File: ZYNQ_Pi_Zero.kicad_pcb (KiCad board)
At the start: 4 copper layers, 59 parts, among them Q501 2N7002, Q502 2N7002, Q503 2N7002, U101 xc7z010clg400, U201 MT41K256M16TW-107_P, U301 W25Q256FVEI, U501 TPD4E05U06DQA, U502 TPD4E05U06DQA

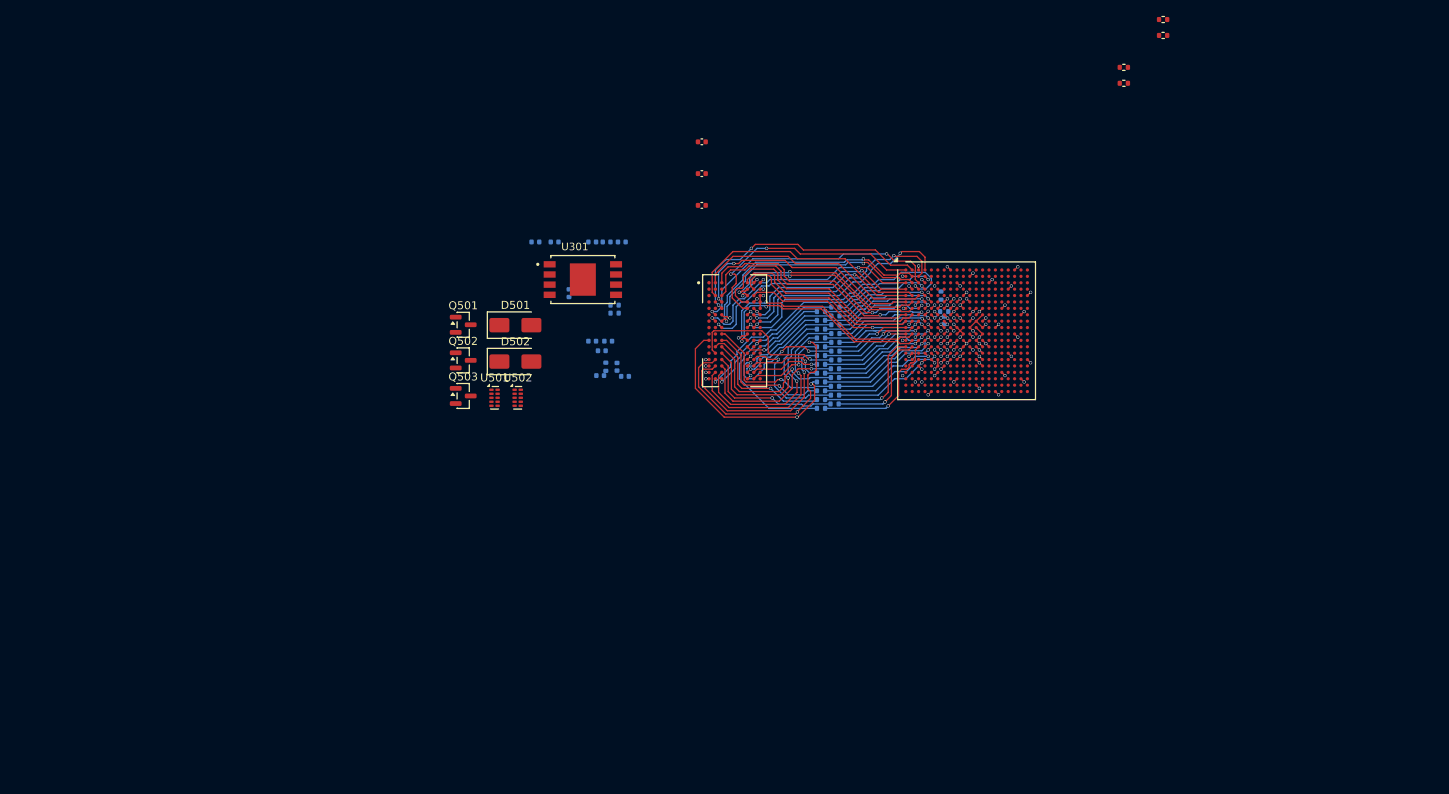
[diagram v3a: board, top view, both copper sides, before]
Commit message: feat: continue routing ddr3
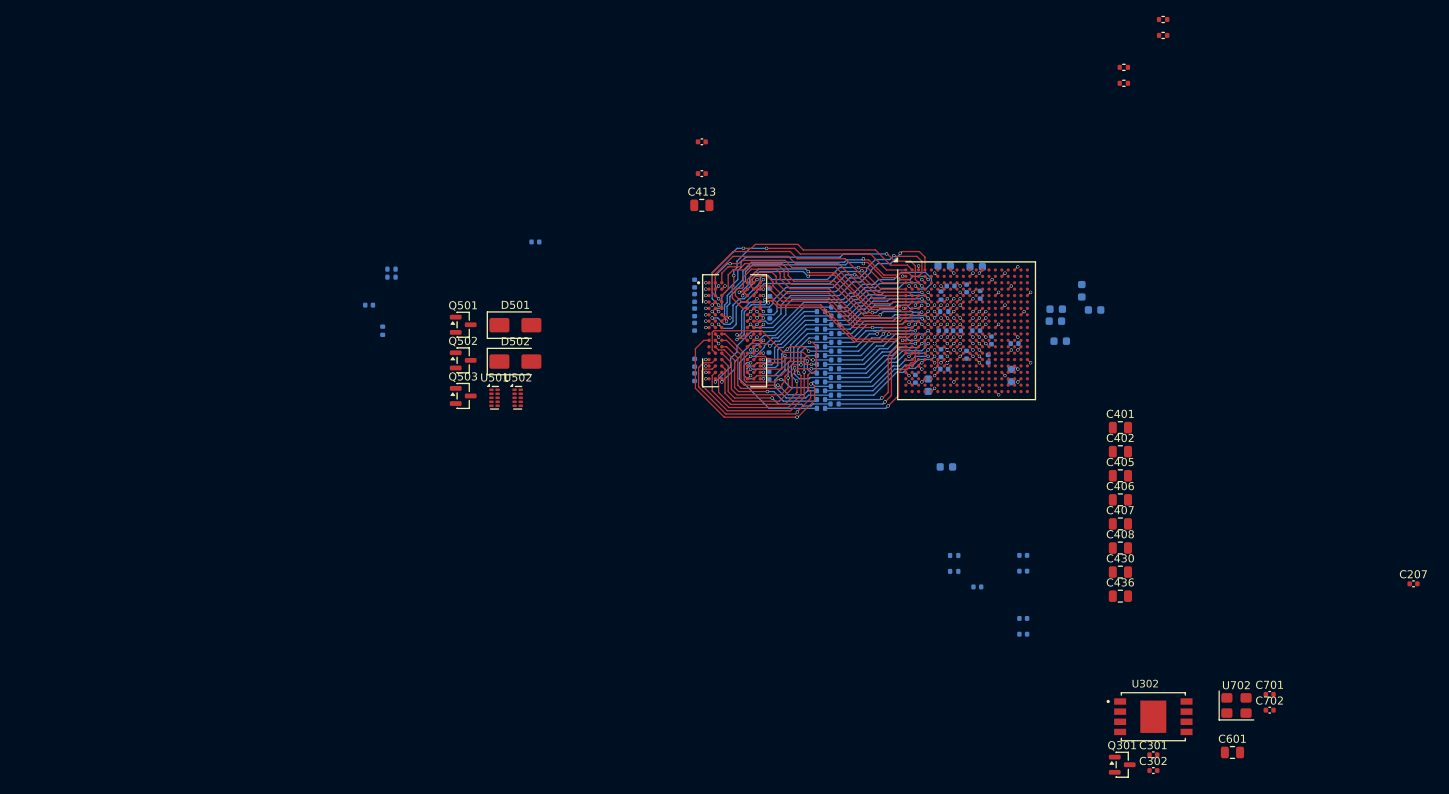
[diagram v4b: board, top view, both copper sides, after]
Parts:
- removed R231: 10R, Resistor_SMD:R_0402_1005Metric
- removed U301: W25Q256FVEI, Footprints:IC_W25N04KVZEIU
- added C207: 100n, Capacitor_SMD:C_0402_1005Metric, F.Cu at (204.9, 131.6)
- added C301: 470n, Capacitor_SMD:C_0402_1005Metric, F.Cu at (172.3, 153.0)
- added C302: 470n, Capacitor_SMD:C_0402_1005Metric, F.Cu at (172.3, 155.0)
- added C401: 10u, Capacitor_SMD:C_0805_2012Metric, F.Cu at (168.2, 112.1)
- added C402: 10u, Capacitor_SMD:C_0805_2012Metric, F.Cu at (168.2, 115.1)
- added C403: 3n3, Capacitor_SMD:C_0402_1005Metric, B.Cu at (156.1, 128.1)
- added C404: 3n3, Capacitor_SMD:C_0402_1005Metric, B.Cu at (156.1, 130.1)
- added C405: 47u, Capacitor_SMD:C_0805_2012Metric, F.Cu at (168.2, 118.1)
- added C406: 10u, Capacitor_SMD:C_0805_2012Metric, F.Cu at (168.2, 121.1)
- added C407: 22u, Capacitor_SMD:C_0805_2012Metric, F.Cu at (168.2, 124.1)
- added C408: 10u, Capacitor_SMD:C_0805_2012Metric, F.Cu at (168.2, 127.2)
- added C409: 4u7, Capacitor_SMD:C_0603_1608Metric, B.Cu at (160.2, 97.3)
- added C410: 4u7, Capacitor_SMD:C_0603_1608Metric, B.Cu at (154.6, 105.6)
- added C411: 470n, Capacitor_SMD:C_0402_1005Metric, B.Cu at (146.2, 104.8)
- added C412: 470n, Capacitor_SMD:C_0402_1005Metric, B.Cu at (155.0, 101.6)
- added C414: 3n3, Capacitor_SMD:C_0402_1005Metric, B.Cu at (156.1, 136.0)
- added C415: 100n, Capacitor_SMD:C_0402_1005Metric, B.Cu at (156.1, 137.9)
- added C416: 4u7, Capacitor_SMD:C_0603_1608Metric, B.Cu at (165.0, 97.4)
- added C417: 4u7, Capacitor_SMD:C_0603_1608Metric, B.Cu at (146.5, 117.0)
- added C418: 470n, Capacitor_SMD:C_0402_1005Metric, B.Cu at (150.2, 100.0)
- added C419: 470n, Capacitor_SMD:C_0402_1005Metric, B.Cu at (149.0, 103.0)
- added C420: 4u7, Capacitor_SMD:C_0603_1608Metric, B.Cu at (160.7, 101.3)
- added C421: 4u7, Capacitor_SMD:C_0603_1608Metric, B.Cu at (146.2, 91.9)
- added C422: 470n, Capacitor_SMD:C_0402_1005Metric, B.Cu at (146.0, 100.0)
- added C423: 470n, Capacitor_SMD:C_0402_1005Metric, B.Cu at (147.0, 94.4)
- added C424: 470n, Capacitor_SMD:C_0402_1005Metric, B.Cu at (145.8, 102.8)
- added C425: 4u7, Capacitor_SMD:C_0603_1608Metric, B.Cu at (160.1, 98.8)
- added C426: 4u7, Capacitor_SMD:C_0603_1608Metric, B.Cu at (150.2, 92.0)
- added C427: 470n, Capacitor_SMD:C_0402_1005Metric, B.Cu at (151.7, 103.5)
- added C428: 470n, Capacitor_SMD:C_0402_1005Metric, B.Cu at (149.0, 94.7)
- added C429: 470n, Capacitor_SMD:C_0402_1005Metric, B.Cu at (152.1, 101.2)
- added C430: 10u, Capacitor_SMD:C_0805_2012Metric, F.Cu at (168.2, 130.2)
- added C431: 470n, Capacitor_SMD:C_0402_1005Metric, B.Cu at (150.3, 132.0)
- added C432: 4u7, Capacitor_SMD:C_0603_1608Metric, B.Cu at (163.4, 95.0)
- added C433: 4u7, Capacitor_SMD:C_0603_1608Metric, B.Cu at (144.2, 106.8)
- added C434: 470n, Capacitor_SMD:C_0402_1005Metric, B.Cu at (147.8, 100.0)
- added C435: 470n, Capacitor_SMD:C_0402_1005Metric, B.Cu at (142.6, 106.0)
- added C436: 22u, Capacitor_SMD:C_0805_2012Metric, F.Cu at (168.2, 133.2)
- added C601: 10u, Capacitor_SMD:C_0805_2012Metric, F.Cu at (182.2, 152.7)
- added C701: 100n, Capacitor_SMD:C_0402_1005Metric, F.Cu at (186.9, 145.5)
- added C702: 470n, Capacitor_SMD:C_0402_1005Metric, F.Cu at (186.9, 147.4)
- added Q301: MMBT3904, Package_TO_SOT_SMD:SOT-23, F.Cu at (168.5, 154.2)
- added R228: 10R, Resistor_SMD:R_0402_1005Metric, B.Cu at (130.8, 106.4)
- added R404: 10k, Resistor_SMD:R_0402_1005Metric, B.Cu at (147.4, 128.1)
- added R409: 10k, Resistor_SMD:R_0402_1005Metric, B.Cu at (147.4, 130.1)
- added U302: W25Q256FVEI, Footprints:IC_W25N04KVZEIU, F.Cu at (172.3, 148.2)
- added U702: 33.3333MHz, Oscillator:Oscillator_SMD_SeikoEpson_SG8002CE-4Pin_3.2x2.5mm, F.Cu at (182.7, 146.8)
- C213: value 100n -> 10n
- C413: value 100n -> 10u; footprint Capacitor_SMD:C_0402_1005Metric -> Capacitor_SMD:C_0805_2012Metric
- R402: value 10k -> 5k1
- R407: value 10k -> 13k
- moved C203 31.6 mm to (124.3, 105.6), turned to -90 degrees
- moved C214 28.3 mm to (74.3, 96.8)
- moved R201 28.3 mm to (76.0, 100.0)
- moved R202 28.3 mm to (77.1, 93.3)
- moved R203 28.3 mm to (77.1, 92.3)
- moved C205 23.1 mm to (124.4, 95.2), turned to 90 degrees
- moved C210 21.5 mm to (124.4, 98.0), turned to -90 degrees
- moved C209 20.2 mm to (124.3, 103.2), turned to 90 degrees
- moved C212 18.9 mm to (115.0, 105.8)
- moved C204 14.2 mm to (115.0, 97.7), turned to -90 degrees
- moved C202 12.2 mm to (115.0, 94.1), turned to 90 degrees
- moved C201 11.5 mm to (115.0, 95.9), turned to -90 degrees
- moved C206 10.9 mm to (115.0, 99.5)
- moved C211 8.86 mm to (115.0, 104.0), turned to -90 degrees
- moved C208 5.52 mm to (150.7, 95.5)
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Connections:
- net /POWER/1V5_PG renamed Net-(J401-CC2)
- C205 pad 2: VTTREF -> GND
- C206 pad 1: VTTREF -> +1V5
- C213 pad 1: +1V5 -> VTTREF
- C214 pad 1: +1V5 -> VTTREF
- R229 pad 1: /DDR3/PS_DDR_ODT -> /DDR3/PS_DDR_~{WE}
- R229 pad 2: /DDR3/DDR_ODT -> /DDR3/DDR_~{WE}
- R230 pad 1: /DDR3/PS_DDR_~{WE} -> /DDR3/PS_DDR_~{RAS}
- R230 pad 2: /DDR3/DDR_~{WE} -> /DDR3/DDR_~{RAS}
- R402 pad 2: +5V -> GND
- R407 pad 1: /POWER/1V8_PG -> +1V5
- R407 pad 2: +5V -> Net-(U402-FB)
- U101 pad A10: (no net) -> unconnected-(U101F-PS_MIO37_501-PadA10)
- U101 pad A11: (no net) -> unconnected-(U101F-PS_MIO36_501-PadA11)
- U101 pad A12: (no net) -> unconnected-(U101F-PS_MIO34_501-PadA12)
- U101 pad A13: (no net) -> +1V8
- U101 pad A14: (no net) -> unconnected-(U101F-PS_MIO32_501-PadA14)
- U101 pad A15: (no net) -> unconnected-(U101F-PS_MIO26_501-PadA15)
- U101 pad A16: (no net) -> unconnected-(U101F-PS_MIO24_501-PadA16)
- U101 pad A17: (no net) -> unconnected-(U101F-PS_MIO20_501-PadA17)
- U101 pad A19: (no net) -> unconnected-(U101F-PS_MIO16_501-PadA19)
- U101 pad A5: (no net) -> Net-(U101E-PS_MIO6_500)
- U101 pad A6: (no net) -> QSPI_D3_PS_MIO5
- U101 pad A7: (no net) -> QSPI_CS
- U101 pad A9: (no net) -> SD_DATA1
- U101 pad B10: (no net) -> PS_SRST_B
- U101 pad B12: (no net) -> unconnected-(U101F-PS_MIO48_501-PadB12)
- U101 pad B13: (no net) -> unconnected-(U101F-PS_MIO50_501-PadB13)
- U101 pad B14: (no net) -> unconnected-(U101F-PS_MIO47_501-PadB14)
- U101 pad B15: (no net) -> SD_DATA3
- U101 pad B16: (no net) -> +1V8
- U101 pad B17: (no net) -> unconnected-(U101F-PS_MIO22_501-PadB17)
- U101 pad B18: (no net) -> unconnected-(U101F-PS_MIO18_501-PadB18)
- U101 pad B5: (no net) -> PS_MIO9
- U101 pad B6: (no net) -> +3V3
- U101 pad B7: (no net) -> QSPI_D2_PS_MIO4
- U101 pad B8: (no net) -> QSPI_D0
- U101 pad B9: (no net) -> unconnected-(U101F-PS_MIO51_501-PadB9)
- U101 pad C10: (no net) -> unconnected-(U101F-PS_MIO52_501-PadC10)
- U101 pad C11: (no net) -> unconnected-(U101F-PS_MIO53_501-PadC11)
- U101 pad C12: (no net) -> unconnected-(U101F-PS_MIO49_501-PadC12)
- U101 pad C13: (no net) -> unconnected-(U101F-PS_MIO29_501-PadC13)
- U101 pad C15: (no net) -> unconnected-(U101F-PS_MIO30_501-PadC15)
- U101 pad C16: (no net) -> unconnected-(U101F-PS_MIO28_501-PadC16)
- U101 pad C17: (no net) -> SD_CMD
- U101 pad C18: (no net) -> unconnected-(U101F-PS_MIO39_501-PadC18)
- U101 pad C19: Net-(U101D-VCCO_35[6]-PadC19) -> +1V8
- U101 pad C5: (no net) -> PS_MIO14
- U101 pad C6: (no net) -> PS_MIO11
- U101 pad C7: (no net) -> PS_POR_B
- U101 pad C8: (no net) -> PS_MIO15
- U101 pad D10: (no net) -> unconnected-(U101F-PS_MIO19_501-PadD10)
- U101 pad D11: (no net) -> unconnected-(U101F-PS_MIO23_501-PadD11)
- U101 pad D12: (no net) -> +1V8
- U101 pad D13: (no net) -> unconnected-(U101F-PS_MIO27_501-PadD13)
- U101 pad D14: (no net) -> Net-(U101F-PS_MIO40_501)
- U101 pad D15: (no net) -> unconnected-(U101F-PS_MIO33_501-PadD15)
- U101 pad D16: (no net) -> unconnected-(U101F-PS_MIO46_501-PadD16)
- U101 pad D5: (no net) -> PS_MIO8
- U101 pad D6: (no net) -> QSPI_D1
- U101 pad D7: (no net) -> +3V3
- U101 pad D8: (no net) -> PS_MIO7
- U101 pad D9: (no net) -> PS_MIO12
- U101 pad E11: (no net) -> Net-(U101F-PS_MIO_VREF_501)
- U101 pad E12: (no net) -> SD_DATA0
- U101 pad E13: (no net) -> unconnected-(U101F-PS_MIO38_501-PadE13)
- U101 pad E14: (no net) -> unconnected-(U101F-PS_MIO17_501-PadE14)
- U101 pad E15: (no net) -> +1V8
- U101 pad E16: (no net) -> unconnected-(U101F-PS_MIO31_501-PadE16)
- U101 pad E6: (no net) -> PS_MIO0
- U101 pad E7: (no net) -> PS_CLK
- U101 pad E8: (no net) -> PS_MIO13
- U101 pad E9: (no net) -> PS_MIO10
- U101 pad F12: (no net) -> unconnected-(U101F-PS_MIO35_501-PadF12)
- U101 pad F13: (no net) -> SD_DATA2
- U101 pad F14: (no net) -> unconnected-(U101F-PS_MIO21_501-PadF14)
- U101 pad F15: (no net) -> unconnected-(U101F-PS_MIO25_501-PadF15)
- U101 pad F18: Net-(U101D-VCCO_35[6]-PadC19) -> +1V8
- U101 pad H14: Net-(U101D-VCCO_35[6]-PadC19) -> +1V8
- U101 pad J17: Net-(U101D-VCCO_35[6]-PadC19) -> +1V8
- U101 pad K20: Net-(U101D-VCCO_35[6]-PadC19) -> +1V8
- U101 pad M16: Net-(U101D-VCCO_35[6]-PadC19) -> +1V8
- U101 pad N19: Net-(U101C-VCCO_34[6]-PadN19) -> +3V3
- U101 pad R15: Net-(U101C-VCCO_34[6]-PadN19) -> +3V3
- U101 pad T18: Net-(U101C-VCCO_34[6]-PadN19) -> +3V3
- U101 pad T8: Net-(U101B-VCCO_13[4]-PadT8) -> +3V3
- U101 pad U11: Net-(U101B-VCCO_13[4]-PadT8) -> +3V3
- U101 pad V14: Net-(U101C-VCCO_34[6]-PadN19) -> +3V3
- U101 pad W17: Net-(U101C-VCCO_34[6]-PadN19) -> +3V3
- U101 pad W7: Net-(U101B-VCCO_13[4]-PadT8) -> +3V3
- U101 pad Y10: Net-(U101B-VCCO_13[4]-PadT8) -> +3V3
- U101 pad Y20: Net-(U101C-VCCO_34[6]-PadN19) -> +3V3
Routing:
- net +1V5: track 8.14 -> 14.4 mm, vias 16 -> 28
- net GND: track 45.6 -> 49.2 mm, vias 58 -> 74
- net +3V3: track 3.06 -> 5.33 mm, vias 4 -> 8
- net +1V8: track 6.79 -> 9.05 mm, vias 10 -> 14
- net /DDR3/DDR_BA1: track 14.8 -> 16.6 mm
- net /DDR3/DDR_D12: track 22.9 -> 24.2 mm
- net +1V0: track 9.62 -> 8.49 mm, vias 11 -> 12
- net /DDR3/DDR_BA0: track 20.4 -> 19.3 mm
- net /DDR3/DDR_CLK_N: track 28.4 -> 29.5 mm
- net /DDR3/DDR_D7: track 24.3 -> 23.2 mm
- net /DDR3/DDR_A14: track 13.1 -> 14.1 mm
- net VTTREF: track 1.13 -> 2.10 mm, vias 2 -> 4
- net /DDR3/DDR_CKE: track 17.1 -> 18.0 mm
- net /DDR3/DDR_A11: track 13.2 -> 14.1 mm
- net /DDR3/DDR_D6: track 30.0 -> 30.8 mm
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
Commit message: feat: continue routing
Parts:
- added D301: LED, LED_SMD:LED_0603_1608Metric, F.Cu at (36.5, 87.1)
- added D302: LED, LED_SMD:LED_0603_1608Metric, F.Cu at (36.5, 89.6)
- added D701: LED, LED_SMD:LED_0603_1608Metric, F.Cu at (39.4, 94.2)
- added D801: LED, LED_SMD:LED_0603_1608Metric, F.Cu at (45.4, 94.2)
- added R206: 80R6, Resistor_SMD:R_0402_1005Metric, F.Cu at (136.5, 101.7)
- added R301: 1k, Resistor_SMD:R_0402_1005Metric, F.Cu at (35.9, 78.8)
- added R302: 330R, Resistor_SMD:R_0402_1005Metric, F.Cu at (35.9, 80.8)
- added R303: 1k, Resistor_SMD:R_0402_1005Metric, F.Cu at (35.9, 82.8)
- added R304: 4k7, Resistor_SMD:R_0402_1005Metric, F.Cu at (35.9, 84.8)
- added R305: 4k7, Resistor_SMD:R_0402_1005Metric, F.Cu at (38.8, 78.8)
- added R306: 390R, Resistor_SMD:R_0402_1005Metric, F.Cu at (38.8, 80.8)
- added R307: 470R, Resistor_SMD:R_0402_1005Metric, F.Cu at (38.8, 82.8)
- added R308: 20k, Resistor_SMD:R_0402_1005Metric, F.Cu at (38.8, 84.8)
- added R309: 20k, Resistor_SMD:R_0402_1005Metric, F.Cu at (41.7, 78.8)
- added R310: 20k, Resistor_SMD:R_0402_1005Metric, F.Cu at (41.7, 80.8)
- added R311: 20k, Resistor_SMD:R_0402_1005Metric, F.Cu at (41.7, 82.8)
- added R312: 20k, Resistor_SMD:R_0402_1005Metric, F.Cu at (41.7, 84.8)
- added R313: 20k, Resistor_SMD:R_0402_1005Metric, F.Cu at (44.6, 78.8)
- added R314: 20k, Resistor_SMD:R_0402_1005Metric, F.Cu at (44.6, 80.8)
- added R315: 20k, Resistor_SMD:R_0402_1005Metric, F.Cu at (44.6, 82.8)
- added R316: 20k, Resistor_SMD:R_0402_1005Metric, F.Cu at (44.6, 84.8)
- added R401: 100k, Resistor_SMD:R_0402_1005Metric, F.Cu at (31.0, 78.8)
- added R403: 5k1, Resistor_SMD:R_0402_1005Metric, F.Cu at (31.0, 80.8)
- added R405: 86k6, Resistor_SMD:R_0402_1005Metric, F.Cu at (31.0, 82.8)
- added R406: 200k, Resistor_SMD:R_0402_1005Metric, F.Cu at (31.0, 84.8)
- added R408: 15k, Resistor_SMD:R_0402_1005Metric, F.Cu at (31.0, 86.8)
- added R410: 18k7, Resistor_SMD:R_0402_1005Metric, F.Cu at (31.0, 88.7)
- added R411: 15k, Resistor_SMD:R_0402_1005Metric, F.Cu at (31.0, 90.7)
- added R506: 4k7, Resistor_SMD:R_0402_1005Metric, F.Cu at (49.5, 78.8)
- added R508: 4k7, Resistor_SMD:R_0402_1005Metric, F.Cu at (49.5, 80.8)
- added R513: 4k7, Resistor_SMD:R_0402_1005Metric, F.Cu at (49.5, 82.8)
- added R514: 4k7, Resistor_SMD:R_0402_1005Metric, F.Cu at (49.5, 84.8)
- added R518: 4k7, Resistor_SMD:R_0402_1005Metric, F.Cu at (49.5, 86.8)
- added R701: 1k, Resistor_SMD:R_0402_1005Metric, F.Cu at (35.9, 93.9)
- added R708: 1k, Resistor_SMD:R_0402_1005Metric, F.Cu at (35.9, 95.9)
- added R709: 1k, Resistor_SMD:R_0402_1005Metric, F.Cu at (35.9, 97.9)
- added R801: 1k, Resistor_SMD:R_0402_1005Metric, F.Cu at (44.8, 96.5)
- C207: moved to B.Cu
- moved C207 91.2 mm to (118.7, 101.7), turned to -90 degrees
- moved R203 40.3 mm to (116.4, 101.3)
- moved R202 39.9 mm to (116.4, 100.4)
- moved R201 37.9 mm to (113.9, 100.9)
- moved C208 33.9 mm to (117.6, 102.7)
- moved R207 1.60 mm to (134.1, 109.2)
- moved R208 1.60 mm to (134.2, 102.5)
- moved R209 1.60 mm to (134.2, 104.8)
- moved R210 1.60 mm to (134.2, 101.5)
- moved R211 1.60 mm to (132.4, 105.3)
- moved R212 1.60 mm to (132.4, 103.1)
- moved R213 1.60 mm to (132.4, 104.2)
- moved R214 1.60 mm to (132.4, 100.9)
- moved R215 1.60 mm to (132.4, 102.0)
- moved R216 1.60 mm to (134.2, 100.3)
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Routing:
- net VTTREF: track 2.10 -> 10.3 mm
- net /DDR3/DDR_A11: track 14.1 -> 20.1 mm
- net /DDR3/DDR_A1: track 16.8 -> 21.2 mm
- net /DDR3/DDR_A3: track 32.3 -> 36.5 mm
- net /DDR3/DDR_A9: track 25.1 -> 28.8 mm
- net /DDR3/DDR_BA2: track 22.3 -> 25.4 mm
- net /DDR3/DDR_A7: track 23.9 -> 27.0 mm
- net /DDR3/DDR_A14: track 14.1 -> 16.8 mm
- net /DDR3/DDR_A5: track 25.1 -> 27.6 mm
- net /DDR3/DDR_ODT: track 27.5 -> 29.5 mm
- net /DDR3/DDR_CKE: track 18.0 -> 19.9 mm
- net /DDR3/PS_DDR_A3: track 10.9 -> 9.06 mm
- net /DDR3/DDR_~{RAS}: track 18.7 -> 20.4 mm
- net /DDR3/DDR_A2: track 19.9 -> 21.6 mm
- net /DDR3/PS_DDR_A13: track 12.3 -> 10.7 mm
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
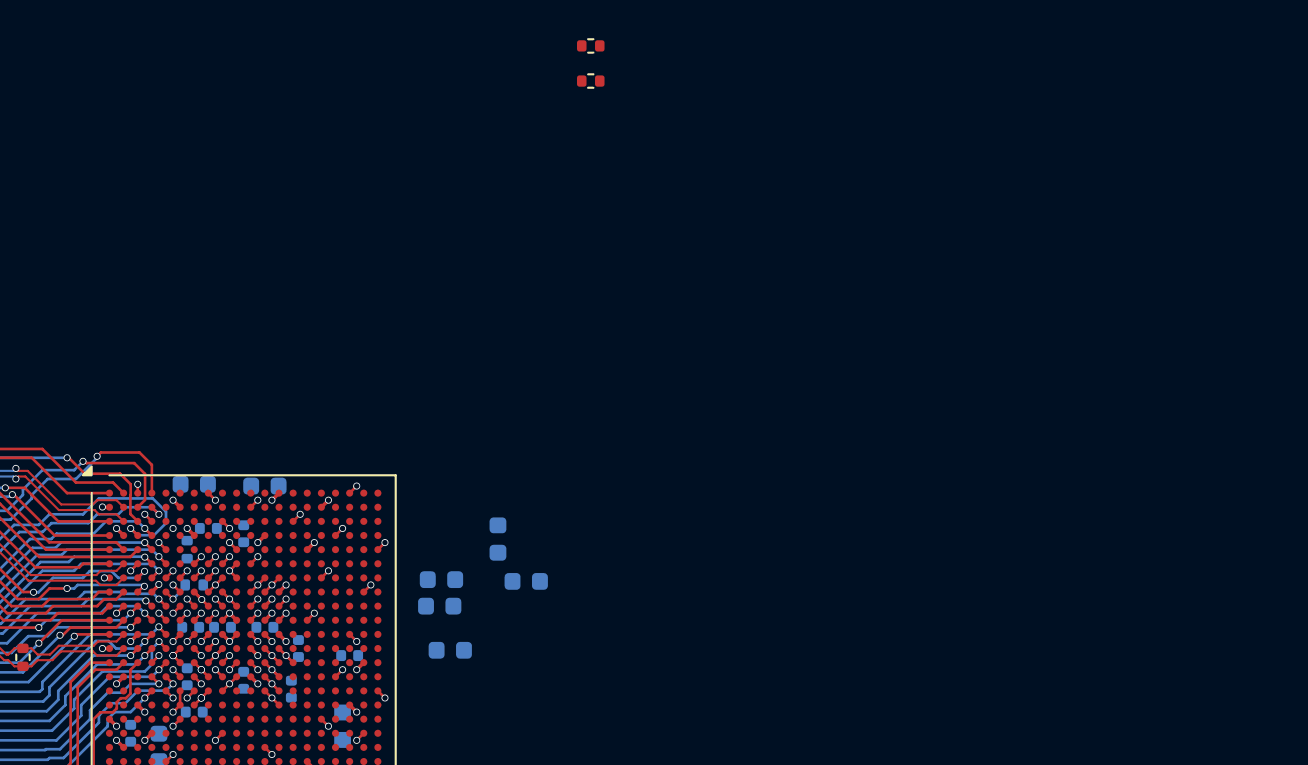
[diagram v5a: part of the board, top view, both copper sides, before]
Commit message: feat: add sd card footprint
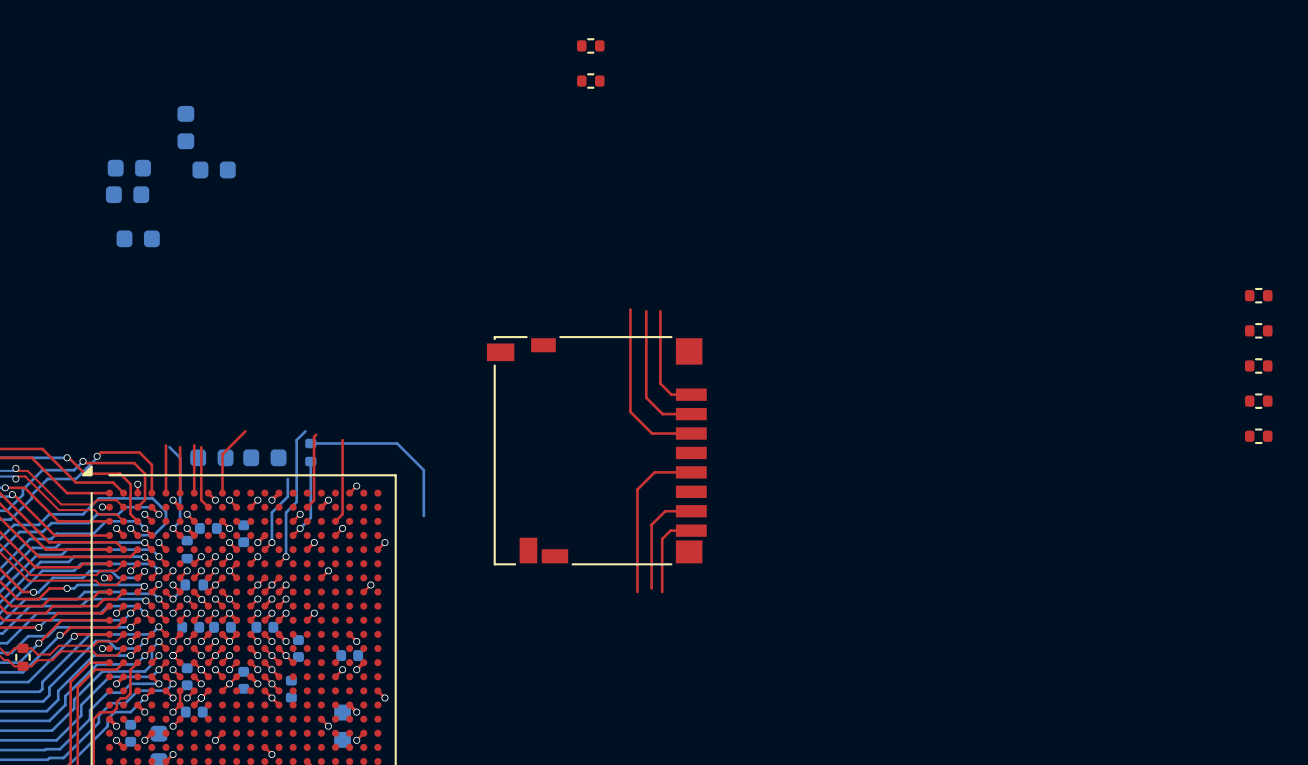
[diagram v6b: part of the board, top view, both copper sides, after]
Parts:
- added J601: Micro_SD_Card, Connector_Card:microSD_HC_Hirose_DM3D-SF, F.Cu at (169.0, 90.0)
- added R601: 47k, Resistor_SMD:R_0402_1005Metric, F.Cu at (206.5, 81.2)
- added R602: 47k, Resistor_SMD:R_0402_1005Metric, F.Cu at (206.5, 83.2)
- added R603: 47k, Resistor_SMD:R_0402_1005Metric, F.Cu at (206.5, 85.2)
- added R604: 47k, Resistor_SMD:R_0402_1005Metric, F.Cu at (206.5, 87.2)
- added R605: 47k, Resistor_SMD:R_0402_1005Metric, F.Cu at (206.5, 89.2)
- added R711: 33R, Resistor_SMD:R_0402_1005Metric, B.Cu at (152.8, 90.1)
- moved C416 29.2 mm to (147.3, 74.1)
- moved C432 29.2 mm to (145.7, 71.7)
- moved C409 29.2 mm to (142.5, 74.0)
- moved C420 29.2 mm to (143.0, 78.0)
- moved C425 29.2 mm to (142.4, 75.5)
- moved C421 1.80 mm to (147.2, 90.4)
- moved C426 1.60 mm to (150.2, 90.4)
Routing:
- net SD_CLK: track 0.00 -> 18.9 mm
- net SD_CMD: track 0.00 -> 14.5 mm
- net SD_DATA2: track 0.00 -> 14.2 mm, vias 0 -> 1
- net SD_DATA3: track 0.00 -> 12.1 mm
- net SD_DATA0: track 0.00 -> 10.7 mm, vias 0 -> 1
- net SD_DATA1: track 0.00 -> 8.89 mm
- net QSPI_D1: track 0.00 -> 5.58 mm, vias 0 -> 1
- net Net-(U101F-PS_MIO40_501): track 0.00 -> 4.60 mm, vias 0 -> 1
- net QSPI_D0: track 0.00 -> 3.57 mm
- net QSPI_CS: track 0.00 -> 2.70 mm
- net Net-(U101E-PS_MIO6_500): track 0.00 -> 2.70 mm
- net QSPI_D3_PS_MIO5: track 0.00 -> 2.60 mm
- net PS_SRST_B: track 0.00 -> 0.57 mm, vias 0 -> 1
- net PS_POR_B: track 0.00 -> 0.57 mm, vias 0 -> 1
- net +1V5: vias 28 -> 27
